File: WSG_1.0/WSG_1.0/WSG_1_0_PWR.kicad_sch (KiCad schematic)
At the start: 42 parts, among them J2 USB_C_Receptacle_USB2.0_16P, J4 Conn_01x02, U10 TPS22916CYFPR, U11 W25N04KVZEIR, U12 USBLC6-2SC6, U7 BQ25180YBGR, U8 TPS63802DLAR, U9 TPS7A2025PDBVR

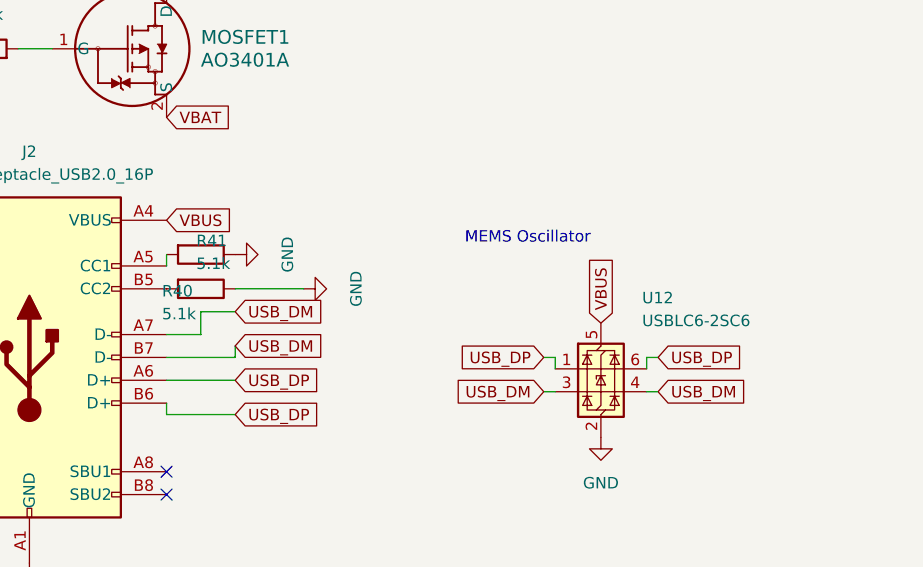
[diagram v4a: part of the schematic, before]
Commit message: adjuts placement slightly, reroute
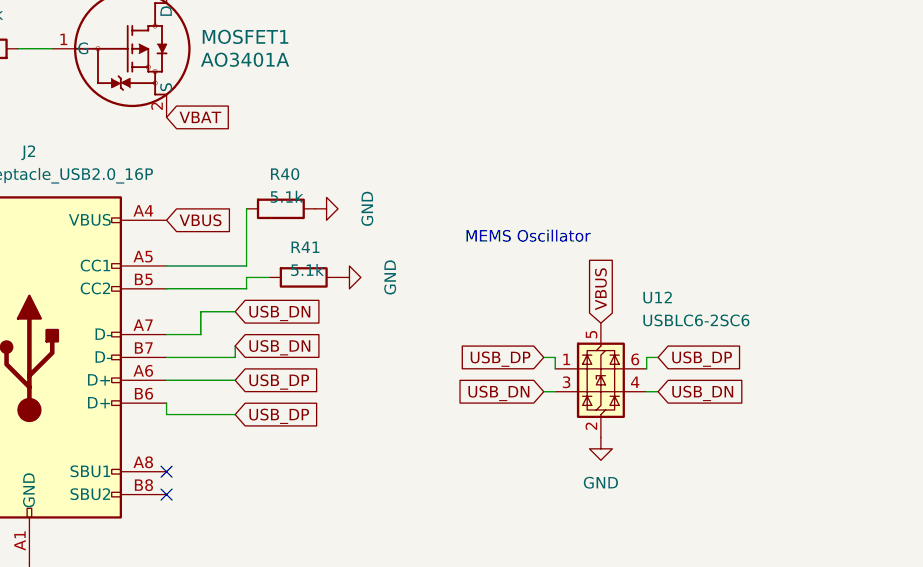
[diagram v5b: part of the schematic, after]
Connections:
- net USB_DM renamed USB_DN
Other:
- moved on the sheet: R40, R41
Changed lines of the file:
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@@
 	(wire
 		(pts
+			(xy 55.88 66.04) (xy 55.88 67.31)
+		)
+		(stroke
+			(width 0)
+			(type default)
+		)
+	)
+	(wire
+		(pts
 			(xy 88.9 139.7) (xy 88.9 138.43)
 		)
@@
 	(wire
 		(pts
+			(xy 58.42 66.04) (xy 55.88 66.04)
+		)
+		(stroke
+			(width 0)
+			(type default)
+		)
+	)
+	(wire
+		(pts
 			(xy 40.64 185.42) (xy 43.18 185.42)
 		)
@@
 	(wire
 		(pts
-			(xy 62.23 67.31) (xy 54.61 67.31)
-		)
-		(stroke
-			(width 0)
-			(type default)
-		)
-	)
-	(wire
-		(pts
 			(xy 113.03 133.35) (xy 129.54 133.35)
 		)
@@
 	(wire
 		(pts
-			(xy 46.99 63.5) (xy 46.99 64.77)
+			(xy 55.88 58.42) (xy 55.88 64.77)
 		)
 		(stroke
@@
 	(wire
 		(pts
+			(xy 55.88 64.77) (xy 46.99 64.77)
+		)
+		(stroke
+			(width 0)
+			(type default)
+		)
+	)
+	(wire
+		(pts
 			(xy 100.33 78.74) (xy 101.6 78.74)
 		)
@@
 	(wire
 		(pts
+			(xy 55.88 67.31) (xy 46.99 67.31)
+		)
+		(stroke
+			(width 0)
+			(type default)
+		)
+	)
+	(wire
+		(pts
 			(xy 156.21 181.61) (xy 161.29 181.61)
 		)
@@
 		)
 	)
-	(global_label "USB_DM"
+	(global_label "USB_DN"
 		(shape input)
 		(at 54.61 73.66 0)
@@
 		)
 	)
-	(global_label "USB_DM"
+	(global_label "USB_DN"
 		(shape input)
 		(at 88.9 78.74 180)
@@
 		)
 	)
-	(global_label "USB_DM"
+	(global_label "USB_DN"
 		(shape input)
 		(at 54.61 69.85 0)
@@
 		)
 	)
-	(global_label "USB_DM"
+	(global_label "USB_DN"
 		(shape input)
 		(at 101.6 78.74 0)
@@
 	(symbol
 		(lib_id "Device:R")
-		(at 50.8 67.31 270)
+		(at 62.23 66.04 270)
 		(unit 1)
 		(body_style 1)
@@
 		(dnp no)
 		(property "Reference" "R41"
-			(at 50.292 61.976 90)
+			(at 60.706 62.738 90)
 			(show_name no)
 			(do_not_autoplace no)
@@
 		)
 		(property "Value" "5.1k"
-			(at 50.292 64.516 90)
+			(at 60.706 65.278 90)
 			(show_name no)
 			(do_not_autoplace no)
@@
 		)
 		(property "Footprint" "Resistor_SMD:R_0402_1005Metric_Pad0.72x0.64mm_HandSolder"
-			(at 50.8 65.532 90)
+			(at 62.23 64.262 90)
 			(hide yes)
 			(show_name no)
@@
 		)
 		(property "Datasheet" ""
-			(at 50.8 67.31 0)
+			(at 62.23 66.04 0)
 			(hide yes)
 			(show_name no)
@@
 		)
 		(property "Description" "Resistor"
-			(at 50.8 67.31 0)
+			(at 62.23 66.04 0)
 			(hide yes)
 			(show_name no)
@@
 	(symbol
 		(lib_id "power:GND")
-		(at 54.61 63.5 90)
+		(at 63.5 58.42 90)
 		(unit 1)
 		(body_style 1)
@@
 		(dnp no)
 		(property "Reference" "#PWR081"
-			(at 60.96 63.5 0)
+			(at 69.85 58.42 0)
 			(hide yes)
 			(show_name no)
@@
 		)
 		(property "Value" "GND"
-			(at 60.452 63.5 0)
+			(at 69.342 58.42 0)
 			(show_name no)
 			(do_not_autoplace no)
@@
 		)
 		(property "Footprint" ""
-			(at 54.61 63.5 0)
+			(at 63.5 58.42 0)
 			(hide yes)
 			(show_name no)
@@
 		)
 		(property "Datasheet" ""
-			(at 54.61 63.5 0)
+			(at 63.5 58.42 0)
 			(hide yes)
 			(show_name no)
@@
 		)
 		(property "Description" "Power symbol creates a global label with name \"GND\" , ground"
-			(at 54.61 63.5 0)
+			(at 63.5 58.42 0)
 			(hide yes)
 			(show_name no)
@@
 	(symbol
 		(lib_id "power:GND")
-		(at 62.23 67.31 90)
+		(at 66.04 66.04 90)
 		(unit 1)
 		(body_style 1)
@@
 		(dnp no)
 		(property "Reference" "#PWR082"
-			(at 68.58 67.31 0)
+			(at 72.39 66.04 0)
 			(hide yes)
 			(show_name no)
@@
 		)
 		(property "Value" "GND"
-			(at 68.072 67.31 0)
+			(at 71.882 66.04 0)
 			(show_name no)
 			(do_not_autoplace no)
@@
 		)
 		(property "Footprint" ""
-			(at 62.23 67.31 0)
+			(at 66.04 66.04 0)
 			(hide yes)
 			(show_name no)
@@
 		)
 		(property "Datasheet" ""
-			(at 62.23 67.31 0)
+			(at 66.04 66.04 0)
 			(hide yes)
 			(show_name no)
@@
 		)
 		(property "Description" "Power symbol creates a global label with name \"GND\" , ground"
-			(at 62.23 67.31 0)
+			(at 66.04 66.04 0)
 			(hide yes)
 			(show_name no)
@@
 	(symbol
 		(lib_id "Device:R")
-		(at 50.8 63.5 270)
+		(at 59.69 58.42 270)
 		(unit 1)
 		(body_style 1)
@@
 		(dnp no)
 		(property "Reference" "R40"
-			(at 46.482 67.564 90)
+			(at 58.42 54.61 90)
 			(show_name no)
 			(do_not_autoplace no)
@@
 		)
 		(property "Value" "5.1k"
-			(at 46.482 70.104 90)
+			(at 58.42 57.15 90)
 			(show_name no)
 			(do_not_autoplace no)
@@
 		)
 		(property "Footprint" "Resistor_SMD:R_0402_1005Metric_Pad0.72x0.64mm_HandSolder"
-			(at 50.8 61.722 90)
+			(at 59.69 56.642 90)
 			(hide yes)
 			(show_name no)
@@
 		)
 		(property "Datasheet" ""
-			(at 50.8 63.5 0)
+			(at 59.69 58.42 0)
 			(hide yes)
 			(show_name no)
@@
 		)
 		(property "Description" "Resistor"
-			(at 50.8 63.5 0)
+			(at 59.69 58.42 0)
 			(hide yes)
 			(show_name no)

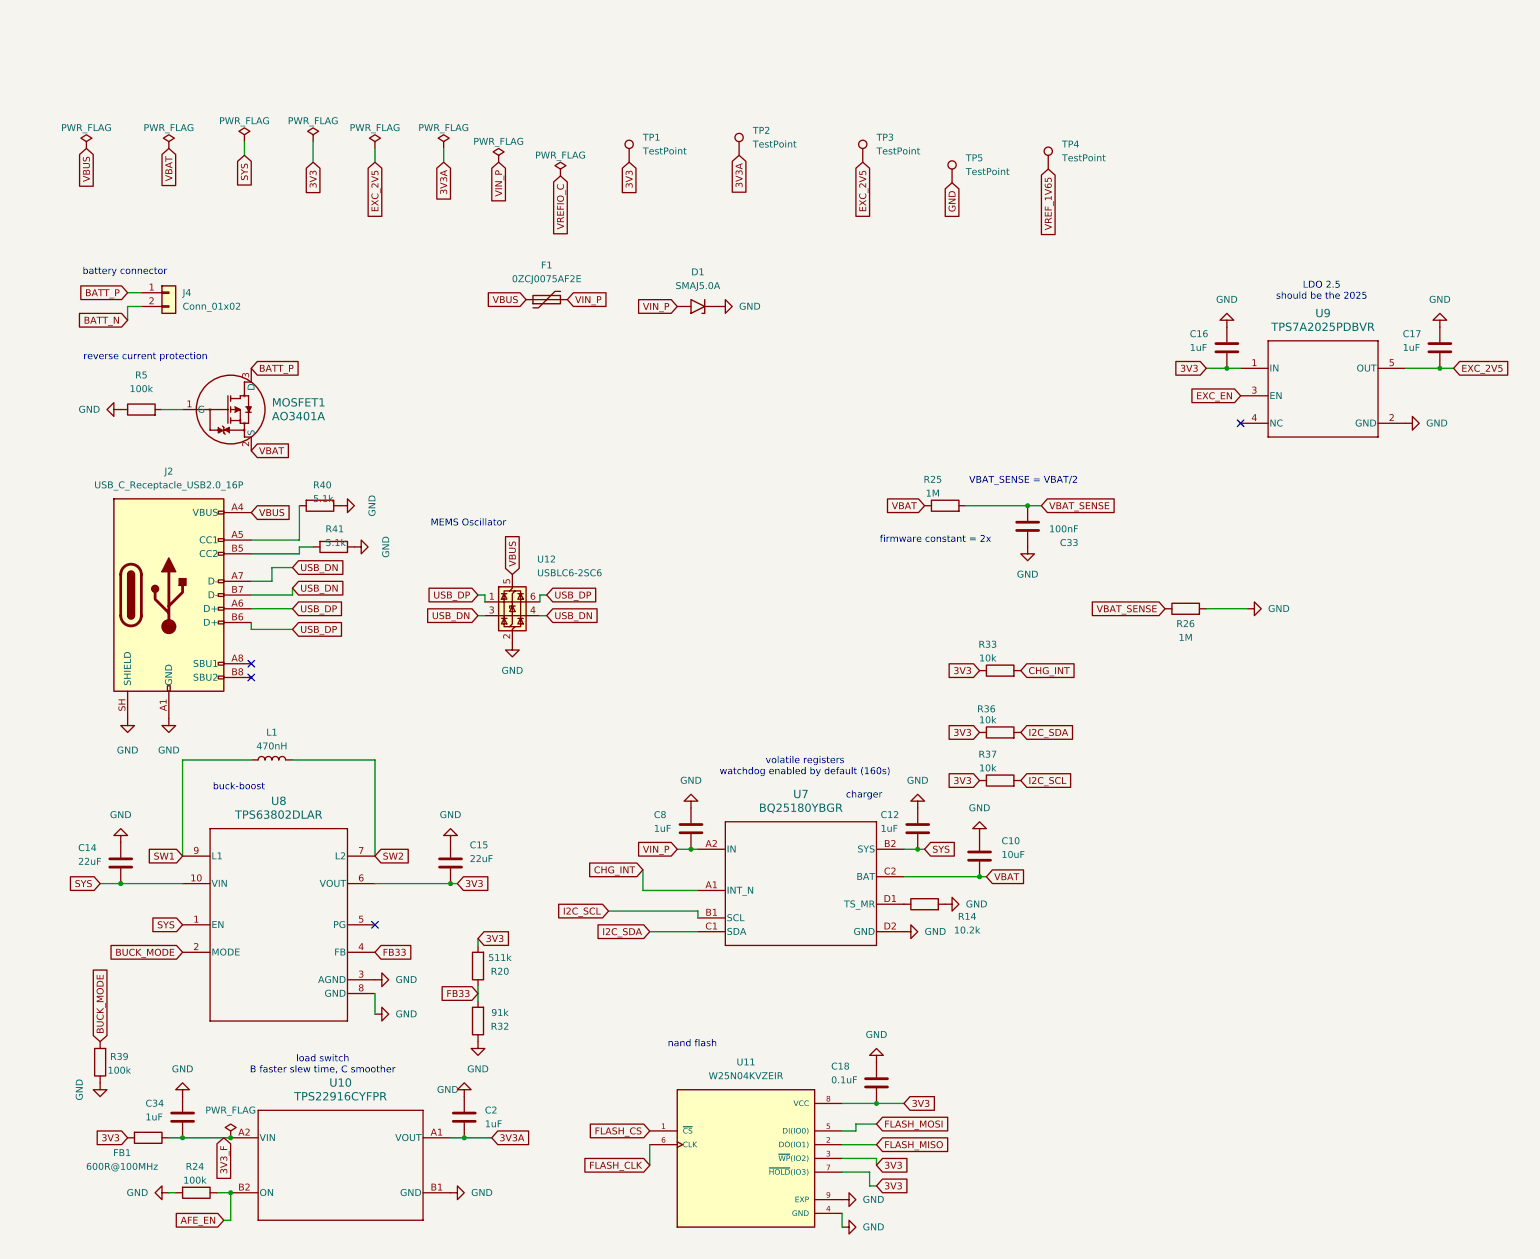
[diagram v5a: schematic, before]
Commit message: cleaned up schematic, starting new layout of pcb
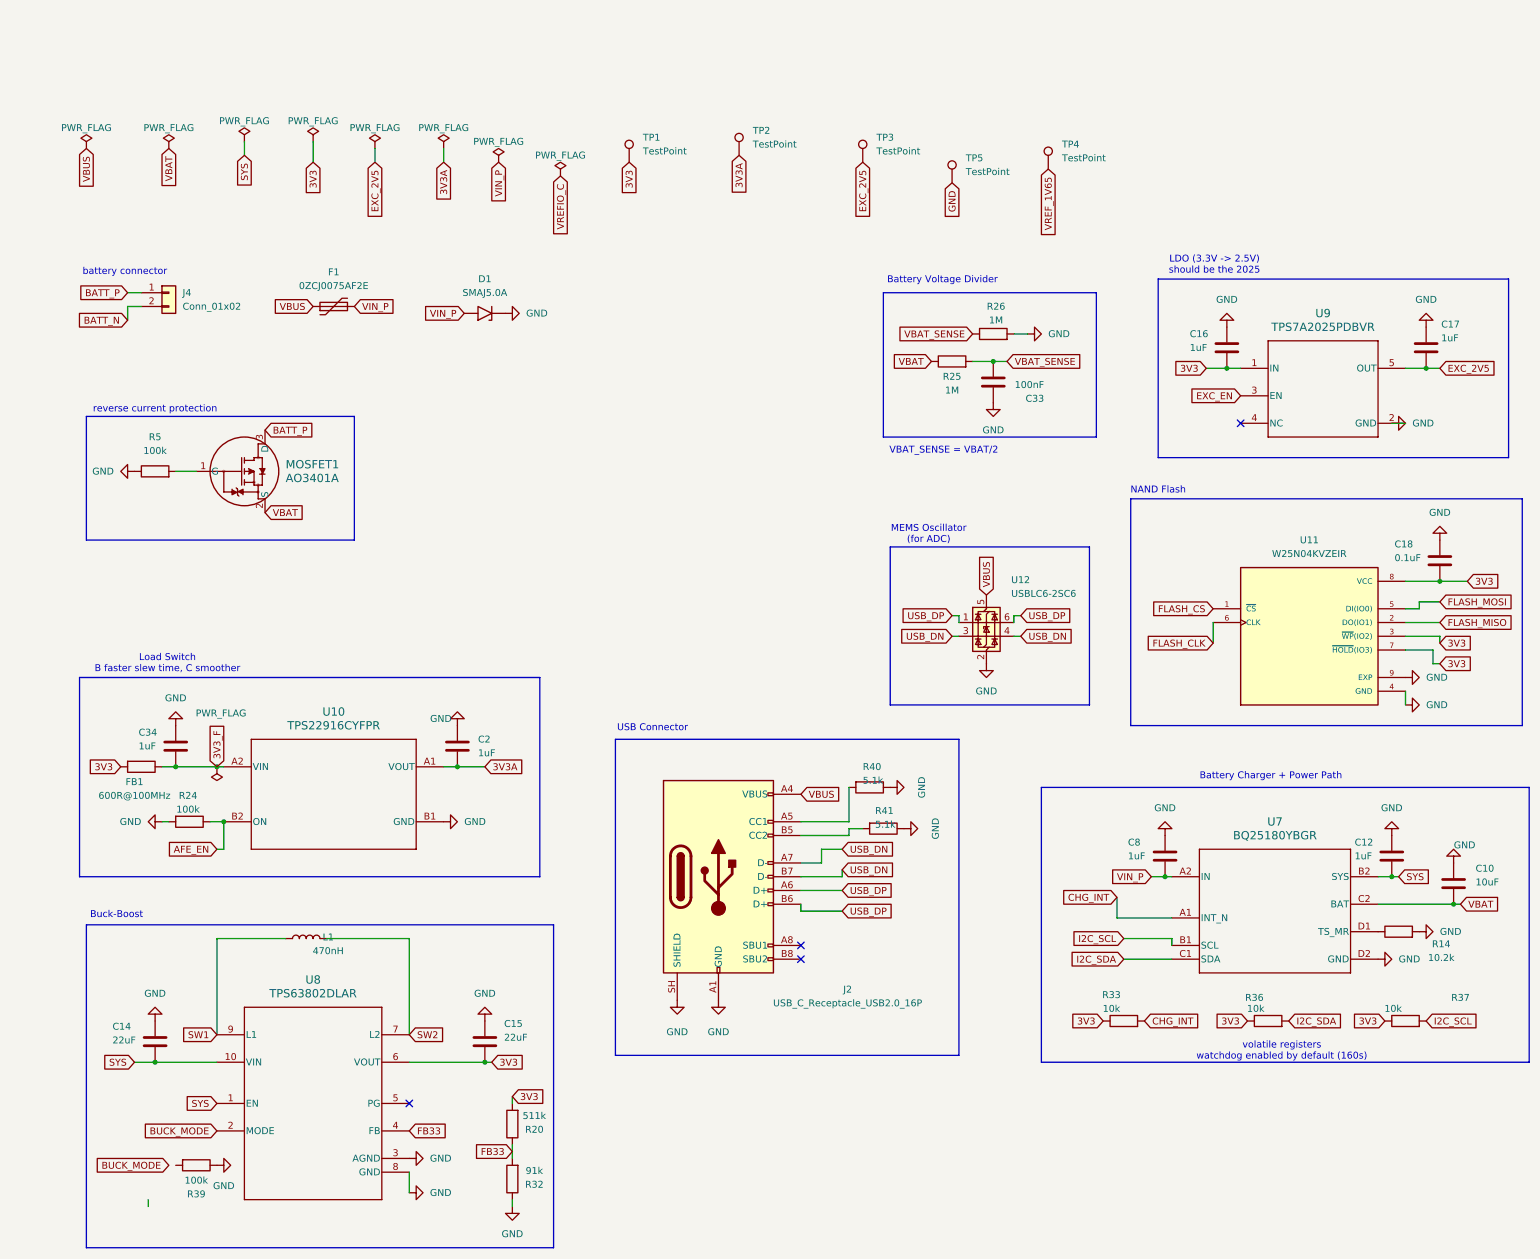
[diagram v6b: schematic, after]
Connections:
- net BUCK_MODE: no longer R39.2
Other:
- note added: "Battery Charger + Power Path"
- note added: "Battery Voltage Divider"
- note added: "Buck-Boost"
- note added: "LDO (3.3V -> 2.5V) should be the 2025"
- note added: "Load Switch B faster slew time, C smoother"
- note added: "MEMS Oscillator (for ADC)"
- note added: "NAND Flash"
- note added: "USB Connector"
- note removed: "LDO 2.5 should be the 2025"
- note removed: "MEMS Oscillator"
- note removed: "buck-boost"
- note removed: "charger"
- note removed: "firmware constant = 2x"
- note removed: "load switch B faster slew time, C smoother"
- note removed: "nand flash"
- moved on the sheet: C10, C12, C14, C15, C17, C18, C2, C33, C34, C8, D1, F1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

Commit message: organized schematic, new layouT
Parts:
- C17: value 1uF -> 10uF; footprint Capacitor_SMD:C_0402_1005Metric_Pad0.74x0.62mm_HandSolder -> Capacitor_SMD:C_0603_1608Metric_Pad1.08x0.95mm_HandSolder; MPN (none) -> GRM188R60J106ME84
- FB1: MPN (none) -> BLM15AG601SN1D
- J2: MPN (none) -> USB4110-GF-A
- L1: MPN XFL4020-471MEC -> XGL4020-471MEC
- MOSFET1: value AO3401A -> DMG2305UX-7
- U11: value W25N04KVZEIR -> W25N02KVZEIR; MP W25N04KVZEIR -> W25N02KVZEIR
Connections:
- net BUCK_MODE: now also R39.2
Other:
- note added: "04KV out of stock, half the capacity"
- note added: "100k = BUCK_MODE pulldown"
- note added: "VBUS -> F1 -> BQ25180 (internal FETs) -> SYS -> TPS63802 -> 3V3 (always-on) -> FB1 -> 3V3_F -> TPS22916C -> 3V3A, 3V3 -> TPS7A2025P -> EXC_2V5 (EN) analog stuff can be turned on and off (is this needed?)"
- note added: "VOUT = 0.5*(1+511k/91k) = 3.31 V"
- note added: "reverse current protection (think this was asked for) no use in normal operation unless battery plugged in wrong"
- note removed: "reverse current protection"
- moved on the sheet: TP1, TP2, TP3, TP4, TP5

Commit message: no drc errors
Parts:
- MOSFET1: value DMG2305UX-7 -> AO3401A
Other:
- note added: "TVS diode"
- note removed: "MEMS Oscillator (for ADC)"
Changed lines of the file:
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@@
 		)
 	)
-	(text "MEMS Oscillator\n(for ADC)"
+	(text "TVS diode"
 		(exclude_from_sim no)
-		(at 172.212 63.754 0)
+		(at 170.434 64.262 0)
 		(effects
 			(font
@@
 			)
 		)
-		(property "Value" "DMG2305UX-7"
+		(property "Value" "AO3401A"
 			(at 53.34 53.3399 0)
 			(show_name no)
